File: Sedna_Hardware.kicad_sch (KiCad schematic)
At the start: 51 parts, among them J1 PJ-102A, J10 5-103634-2, J11 2-644488-2, J2 61201021721, J3 PPTC141LFBN-RC, J4 0878340619, J5 2-644803-3, J6 2-644488-3, J7 1935161, J8 1935161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

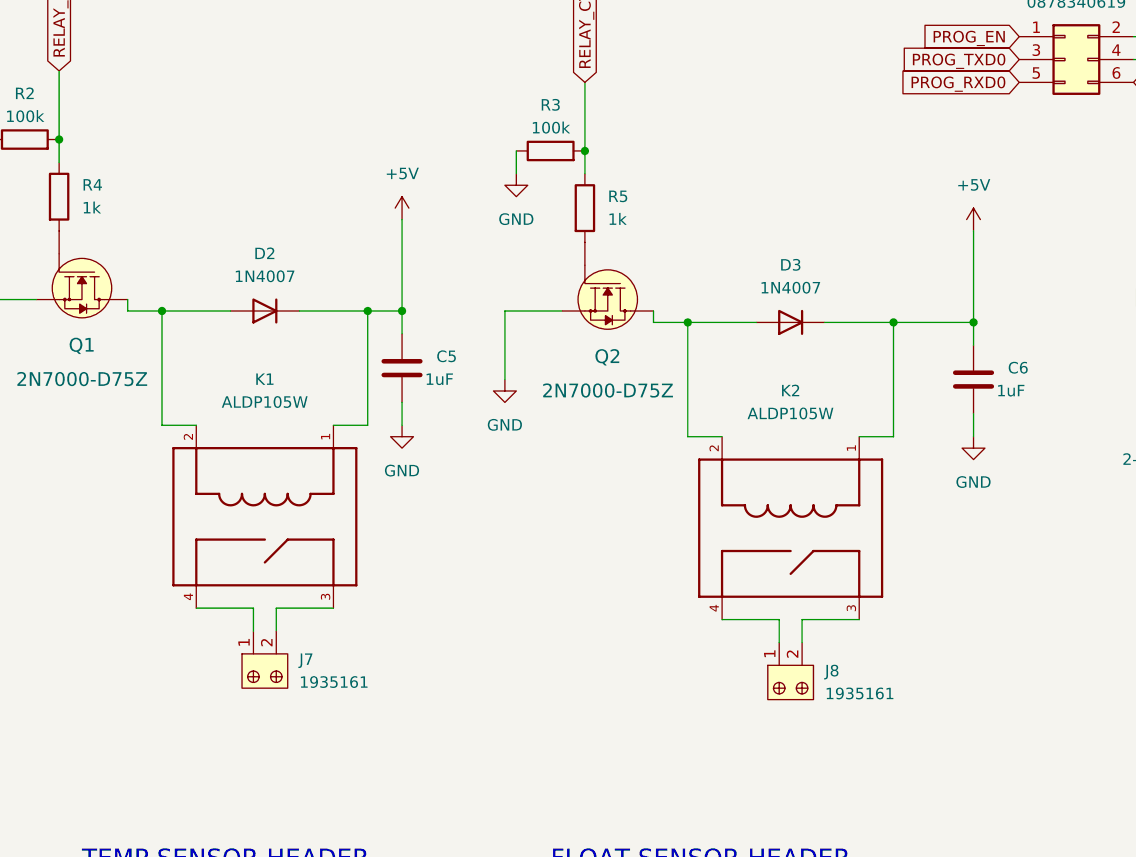
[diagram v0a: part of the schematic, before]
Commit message: modified relay due to stock issues
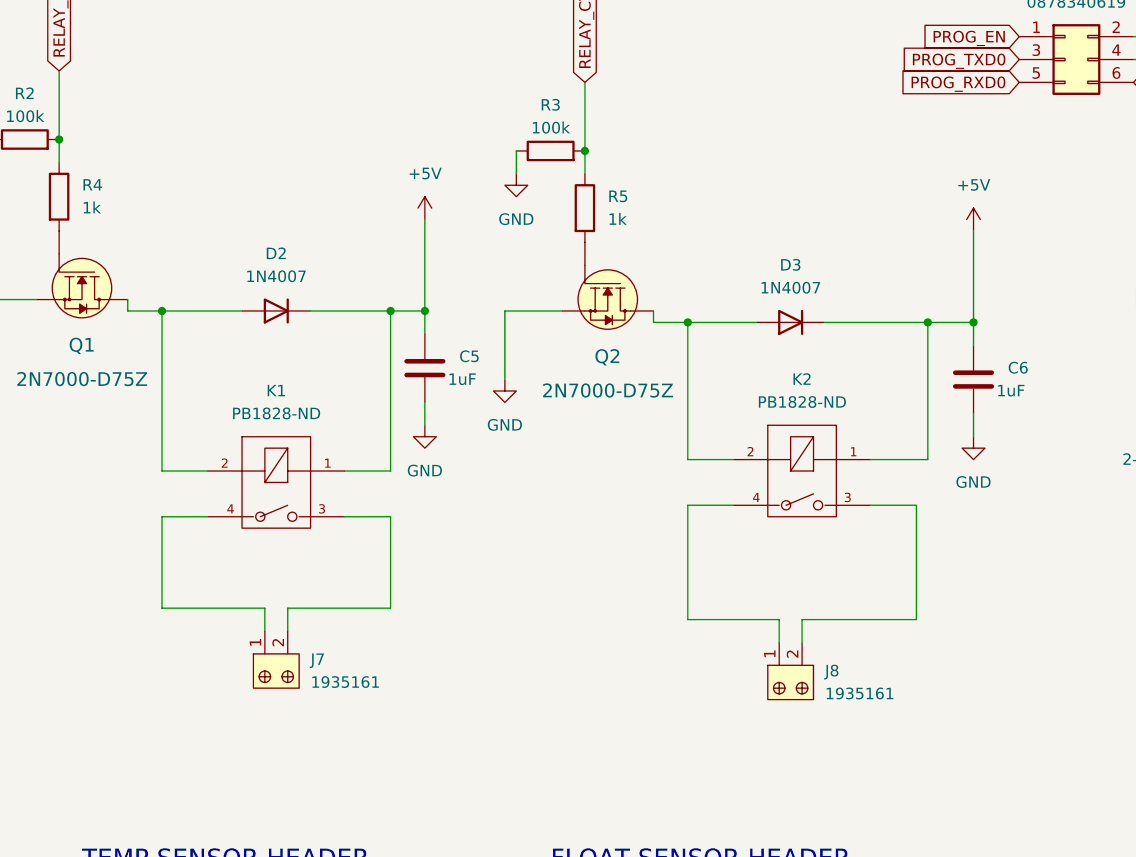
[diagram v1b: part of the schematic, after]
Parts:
- removed K1, K2: ALDP105W, RELAY_ALDP105W, symbol ALDP105W:ALDP105W
- added K1, K2: PB1828-ND, eec:TE_Connectivity-1461352-2-MFG, symbol eec:1461352-2
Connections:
- net +5V: now also K1.1, K2.1
- net at D2.2 (A), Q1.3 (D): now also K1.2
- net at D3.2 (A), Q2.3 (D): now also K2.2
- net at J8.2: now also K2.3
- net at J8.1: now also K2.4
- net at J7.1: now also K1.4
- net at J7.2: now also K1.3
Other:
- moved on the sheet: C5, D2, J7

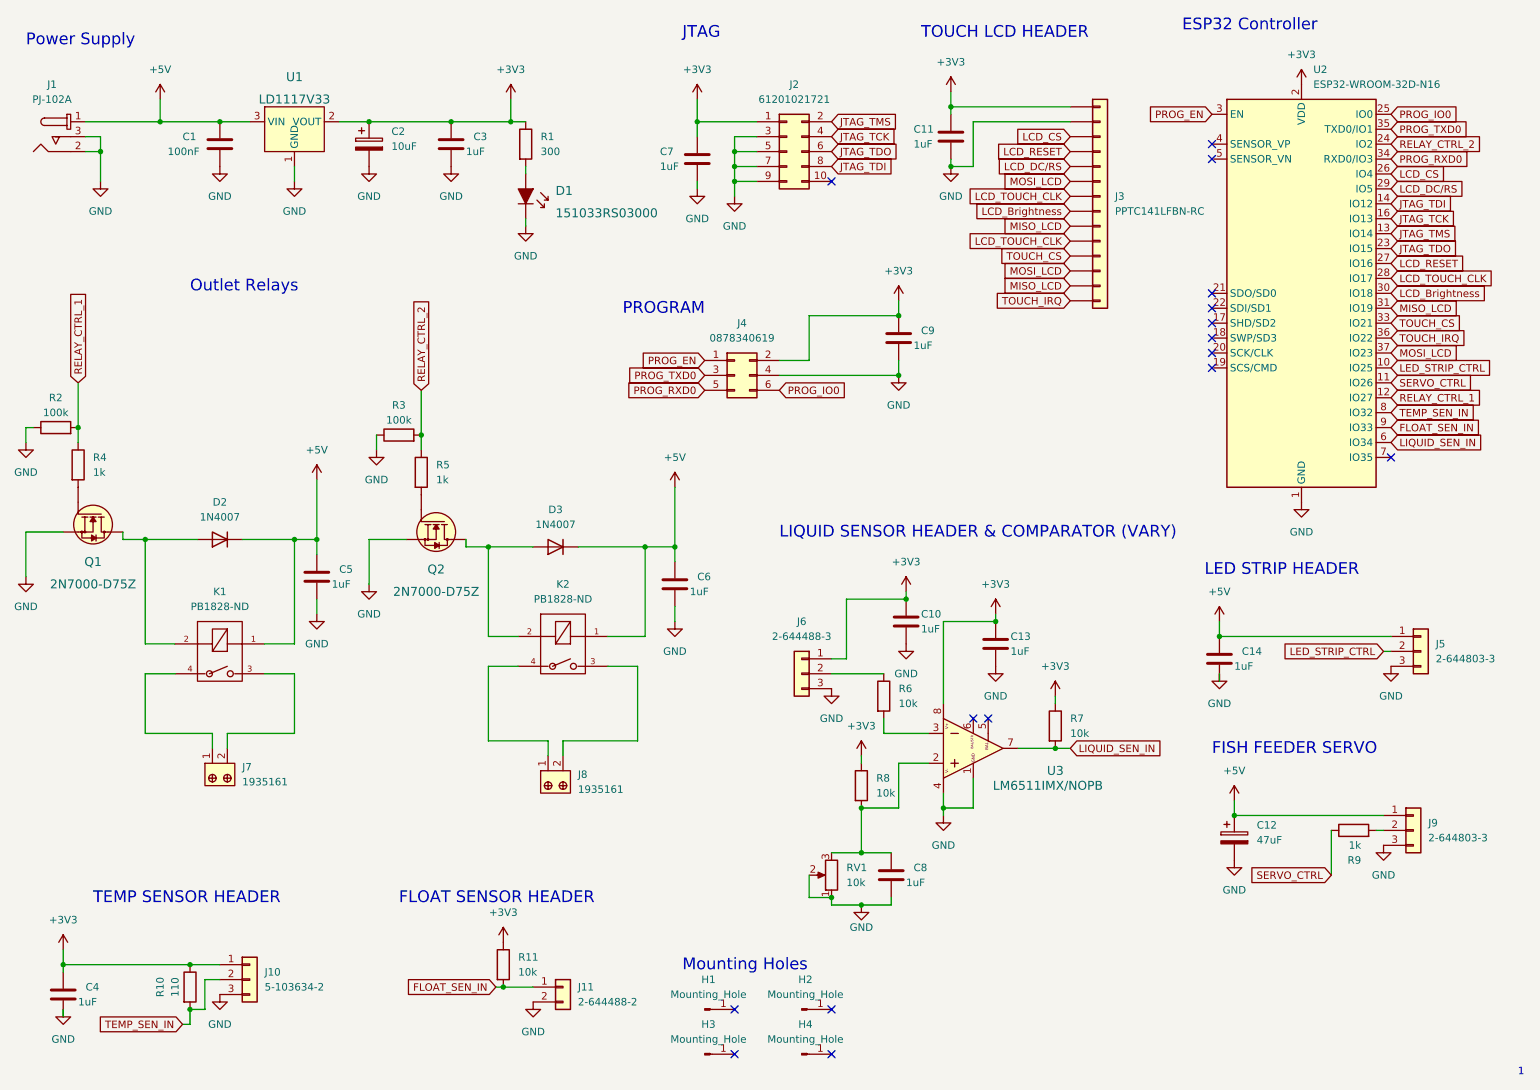
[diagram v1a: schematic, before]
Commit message: updated connector properties
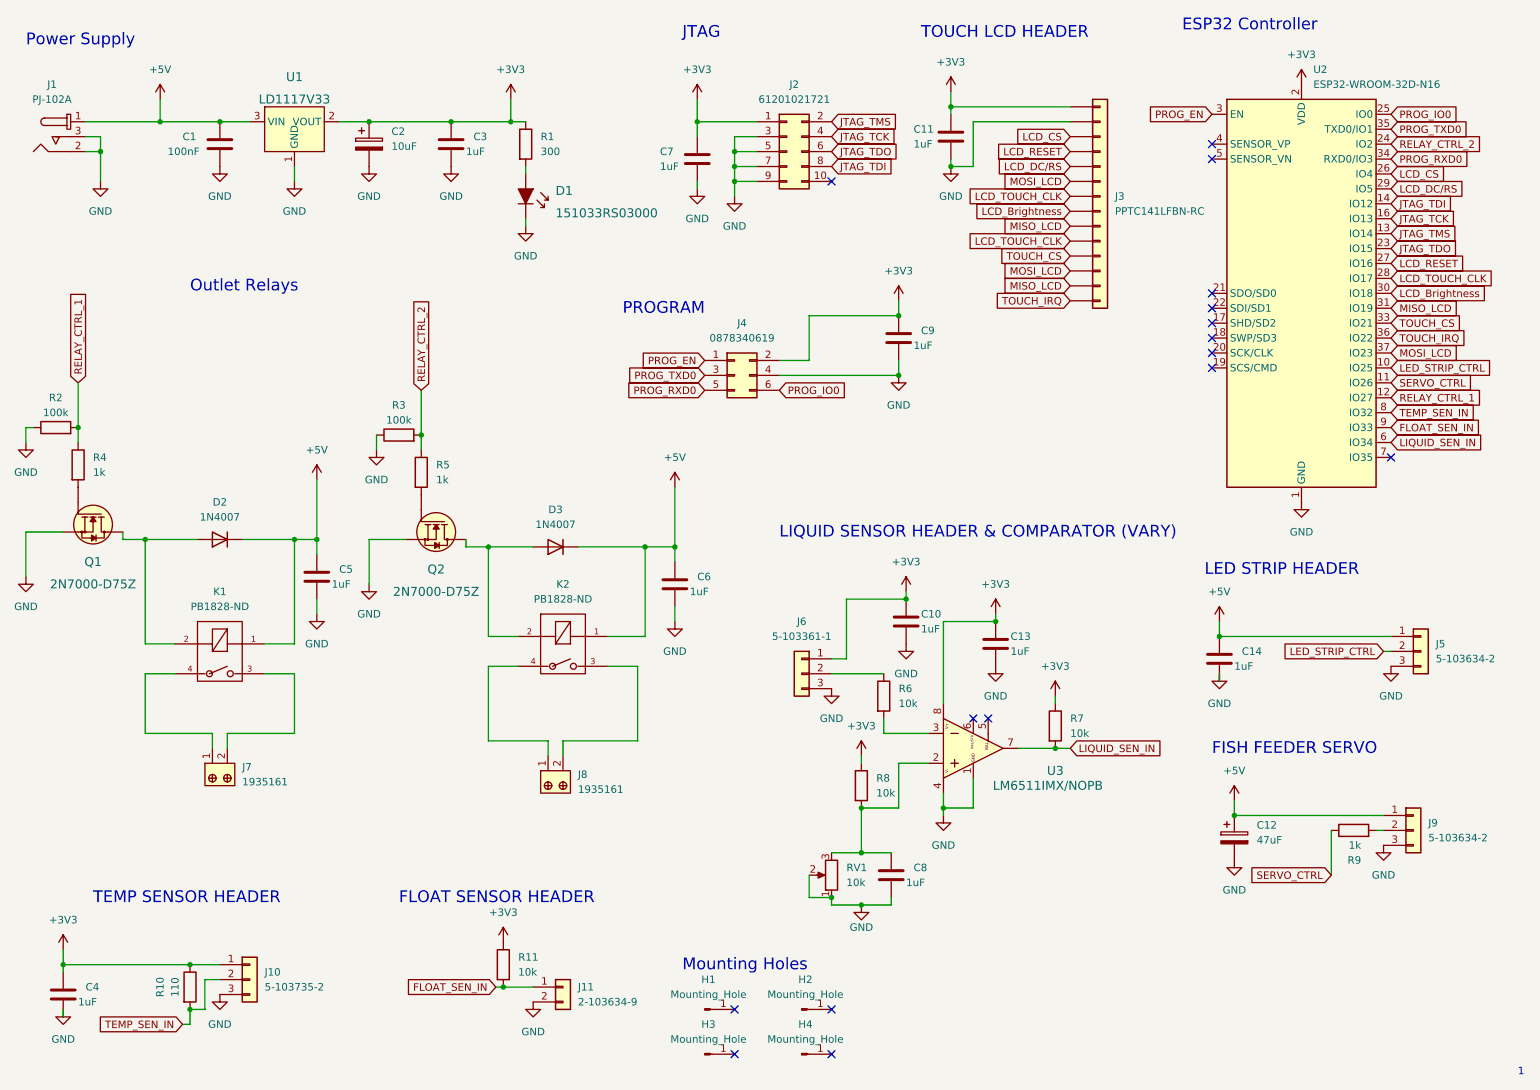
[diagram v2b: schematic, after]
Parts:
- J10: value 5-103634-2 -> 5-103735-2; Category CONN HEADER R/A 3POS 2.54MM -> CONN; DK_Datasheet_Link https://www.te.com/commerce/DocumentDelivery/DDEController?Action=srchrtrv&DocNm=103634&DocType=Customer+Drawing&DocLang=English -> https://www.te.com/commerce/DocumentDelivery/DDEController?Action=srchrtrv&DocNm=103735&DocType=Customer+Drawing&DocLang=English; DK_Detail_Page https://www.digikey.ca/en/products/detail/te-connectivity-amp-connectors/5-103634-2/1122423 -> https://www.digikey.ca/en/products/detail/te-connectivity-amp-connectors/5-103735-2/1122487; Digi-Key_PN A33859-ND -> A33924-ND; MPN 5-103634-2 -> 5-103735-2; Mating_CONN 487526-2 -> 5-103735-2; Mating_DK_Page https://www.digikey.ca/en/products/detail/te-connectivity-amp-connectors/487526-2/293387 -> https://www.digikey.ca/en/products/detail/te-connectivity-amp-connectors/5-103735-2/1122487; Mating_MPN 487526-2 -> 5-103735-2
- J11: value 2-644488-2 -> 2-103634-9; DK_Datasheet_Link https://www.te.com/commerce/DocumentDelivery/DDEController?Action=srchrtrv&DocNm=644488&DocType=Customer+Drawing&DocLang=English -> https://www.te.com/commerce/DocumentDelivery/DDEController?Action=srchrtrv&DocNm=103634&DocType=Customer+Drawing&DocLang=English; DK_Detail_Page https://www.digikey.ca/en/products/detail/te-connectivity-amp-connectors/2-644488-2/698426?s=N4IgTCBcDa4LQDYAsKAcq4QLoF8g -> https://www.digikey.ca/en/products/detail/te-connectivity-amp-connectors/2-103634-9/1889533; Digi-Key_PN A30900-ND -> 2-103634-9-ND; MPN 2-644488-2 -> 2-103634-9; Mating_CONN 3-644043-2 -> 2-103634-9; Mating_DK_Page https://www.digikey.ca/en/products/detail/te-connectivity-amp-connectors/3-644043-2/1863034 -> https://www.digikey.ca/en/products/detail/te-connectivity-amp-connectors/2-103634-9/1889533; Mating_MPN 3-644043-2 -> 2-103634-9
- J5, J9: value 2-644803-3 -> 5-103634-2; DK_Datasheet_Link https://www.te.com/commerce/DocumentDelivery/DDEController?Action=srchrtrv&DocNm=644803&DocType=Customer+Drawing&DocLang=English -> https://www.te.com/commerce/DocumentDelivery/DDEController?Action=srchrtrv&DocNm=103634&DocType=Customer+Drawing&DocLang=English; DK_Detail_Page https://www.digikey.ca/en/products/detail/te-connectivity-amp-connectors/2-644803-3/698440 -> https://www.digikey.ca/en/products/detail/te-connectivity-amp-connectors/5-103634-2/1122423; Digi-Key_PN A30925-ND -> A33859-ND; MPN 2-644803-3 -> 5-103634-2; Mating_CONN 3-640469-3 -> 5-103634-2; Mating_DK_Page https://www.digikey.ca/en/products/detail/te-connectivity-amp-connectors/3-640469-3/1863570 -> https://www.digikey.ca/en/products/detail/te-connectivity-amp-connectors/5-103634-2/1122423; Mating_MPN 3-640469-3 -> 5-103634-2
- J6: value 2-644488-3 -> 5-103361-1; DK_Datasheet_Link https://www.te.com/commerce/DocumentDelivery/DDEController?Action=srchrtrv&DocNm=644488&DocType=Customer+Drawing&DocLang=English -> https://www.te.com/commerce/DocumentDelivery/DDEController?Action=srchrtrv&DocNm=103361&DocType=Customer+Drawing&DocLang=English; DK_Detail_Page https://www.digikey.ca/en/products/detail/te-connectivity-amp-connectors/2-644488-3/698427?s=N4IgTCBcDa4LQDYAsKAcq4GYQF0C%2BQA -> https://www.digikey.ca/en/products/detail/te-connectivity-amp-connectors/5-103361-1/760140; Digi-Key_PN A30901-ND -> A35068-ND; MPN 2-644488-3 -> 5-103361-1; Mating_CONN 3-640468-3 -> 5-103361-1; Mating_DK_Page https://www.digikey.ca/en/products/detail/te-connectivity-amp-connectors/3-640468-3/1863562 -> https://www.digikey.ca/en/products/detail/te-connectivity-amp-connectors/5-103361-1/760140; Mating_MPN 3-640468-3 -> 5-103361-1
